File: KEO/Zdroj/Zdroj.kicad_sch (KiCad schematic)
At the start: 64 parts, among them J1 24V AC, J2 OUT, J3 Q7, Q1 BC547, Q2 BC547, Q3 BC557, Q4 BC557, Q5 BC547, Q6 BD139, Q7 2N3055, U1 TL082, U2 TL082

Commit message: OSY hw05
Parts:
- added R22, R23: 2,2K, symbol Device:R
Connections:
- net GND: now also R23.2; no longer U2.5 (+), U2.6 (-)
- net at C10.2, C7.2, C9.1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: now also R18.2; no longer R18.1
- net at C2.1, C3.2, C4.2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: now also R18.1; no longer R18.2
- net at C8.2, U1.7: now also R19.2; no longer R19.1
- net at D14.1 (K), Q5.1 (C), Q6.3 (B): now also R19.1; no longer R19.2
- net at U2.7: now also U2.6 (-)
- new net: R22.2, R23.1, U2.5 (+)
- no-connect marks 1 -> 0
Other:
- moved on the sheet: H1, H2, H3, H4, R18, R19, U2B

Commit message: OSY hw06
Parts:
- added FID1, FID2, FID3: Fiducial, Fiducial:Fiducial_0.5mm_Mask1mm, symbol Mechanical:Fiducial
- C1, C2, C4: footprint (none) -> Capacitor_THT:C_Radial_D10.0mm_H12.5mm_P5.00mm
- R1, R10, R11, R12, R13, R14, R15, R16, R17, R19, R2, R20, R21, R22, R23, R3, R4, R5, R6, R7, R8, R9, RV1, RV2: footprint (none) -> Resistor_THT:R_Axial_DIN0207_L6.3mm_D2.5mm_P7.62mm_Horizontal
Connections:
- net GND: now also C2.1, C3.2, C4.2, C5.1, C5.2, D12.2 (A), D2.2 (A), D4.2 (A), D5.1 (K), D7.2 (A), D8.1 (K), D9.1 (K), Q4.3 (E), Q5.3 (E), R10.2, R18.1, R2.2, U1.4 (V-), U2.4 (V-)
- net U1,U2+: now reaches C4.1, Q1.3 (E), Q2.2 (B), R17.1, U1.8 (V+), U2.8 (V+)
- net U1,U2+: now also R22.1
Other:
- moved on the sheet: J1

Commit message: Update Zdroj.kicad_sch
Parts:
- C10, C5: footprint (none) -> Capacitor_THT:C_Radial_D6.3mm_H5.0mm_P2.50mm
- C11, C6, C8: footprint (none) -> Capacitor_THT:C_Disc_D5.0mm_W2.5mm_P5.00mm
- C3: footprint (none) -> Capacitor_THT:C_Radial_D16.0mm_H25.0mm_P7.50mm
- C7, C9: footprint (none) -> Capacitor_THT:C_Rect_L7.0mm_W2.5mm_P5.00mm
- D10, D12, D7, D9: footprint (none) -> Diode_THT:D_DO-35_SOD27_P7.62mm_Horizontal
- J1, J2: footprint (none) -> TerminalBlock_Phoenix:TerminalBlock_Phoenix_MKDS-3-2-5.08_1x02_P5.08mm_Horizontal
- J3: footprint (none) -> TerminalBlock_Phoenix:TerminalBlock_Phoenix_MKDS-1,5-3-5.08_1x03_P5.08mm_Horizontal
- R10, RV1, RV2: footprint Resistor_THT:R_Axial_DIN0207_L6.3mm_D2.5mm_P7.62mm_Horizontal -> (none)
- R18: footprint (none) -> Resistor_THT:R_Axial_Power_L25.0mm_W6.4mm_P30.48mm
- U1, U2: footprint (none) -> Package_DIP:DIP-8_W7.62mm
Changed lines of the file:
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@@
 			)
 		)
-		(property "Footprint" "Resistor_THT:R_Axial_DIN0207_L6.3mm_D2.5mm_P7.62mm_Horizontal"
+		(property "Footprint" ""
 			(at 129.54 88.9 0)
 			(effects
@@
 			)
 		)
-		(property "Footprint" ""
+		(property "Footprint" "TerminalBlock_Phoenix:TerminalBlock_Phoenix_MKDS-1,5-3-5.08_1x03_P5.08mm_Horizontal"
 			(at 256.54 39.37 0)
 			(effects
@@
 			)
 		)
-		(property "Footprint" ""
+		(property "Footprint" "Package_DIP:DIP-8_W7.62mm"
 			(at 173.99 92.71 0)
 			(effects
@@
 			)
 		)
-		(property "Footprint" ""
+		(property "Footprint" "Capacitor_THT:C_Radial_D16.0mm_H25.0mm_P7.50mm"
 			(at 69.5452 82.55 0)
 			(effects
@@
 			)
 		)
-		(property "Footprint" ""
+		(property "Footprint" "Capacitor_THT:C_Disc_D5.0mm_W2.5mm_P5.00mm"
 			(at 267.97 86.0552 0)
 			(effects
@@
 			)
 		)
-		(property "Footprint" ""
+		(property "Footprint" "Capacitor_THT:C_Disc_D5.0mm_W2.5mm_P5.00mm"
 			(at 214.9348 77.47 0)
 			(effects
@@
 			)
 		)
-		(property "Footprint" ""
+		(property "Footprint" "Diode_THT:D_DO-35_SOD27_P7.62mm_Horizontal"
 			(at 92.71 115.57 0)
 			(effects
@@
 			)
 		)
-		(property "Footprint" ""
+		(property "Footprint" "Diode_THT:D_DO-35_SOD27_P7.62mm_Horizontal"
 			(at 224.79 124.46 0)
 			(effects
@@
 			)
 		)
-		(property "Footprint" ""
+		(property "Footprint" "Capacitor_THT:C_Rect_L7.0mm_W2.5mm_P5.00mm"
 			(at 191.4652 92.71 0)
 			(effects
@@
 			)
 		)
-		(property "Footprint" ""
+		(property "Footprint" "TerminalBlock_Phoenix:TerminalBlock_Phoenix_MKDS-3-2-5.08_1x02_P5.08mm_Horizontal"
 			(at 281.94 111.76 0)
 			(effects
@@
 			)
 		)
-		(property "Footprint" ""
+		(property "Footprint" "Package_DIP:DIP-8_W7.62mm"
 			(at 154.94 152.4 0)
 			(effects
@@
 			)
 		)
-		(property "Footprint" ""
+		(property "Footprint" "Diode_THT:D_DO-35_SOD27_P7.62mm_Horizontal"
 			(at 69.85 50.8 0)
 			(effects
@@
 			)
 		)
-		(property "Footprint" "Resistor_THT:R_Axial_DIN0207_L6.3mm_D2.5mm_P7.62mm_Horizontal"
+		(property "Footprint" ""
 			(at 127.762 105.41 90)
 			(effects
@@
 			)
 		)
-		(property "Footprint" ""
+		(property "Footprint" "Package_DIP:DIP-8_W7.62mm"
 			(at 111.76 91.44 0)
 			(effects
@@
 			)
 		)
-		(property "Footprint" ""
+		(property "Footprint" "Capacitor_THT:C_Radial_D6.3mm_H5.0mm_P2.50mm"
 			(at 105.1052 119.38 0)
 			(effects
@@
 			)
 		)
-		(property "Footprint" ""
+		(property "Footprint" "TerminalBlock_Phoenix:TerminalBlock_Phoenix_MKDS-3-2-5.08_1x02_P5.08mm_Horizontal"
 			(at 21.59 76.2 0)
 			(effects
@@
 			)
 		)
-		(property "Footprint" ""
+		(property "Footprint" "Package_DIP:DIP-8_W7.62mm"
 			(at 209.55 74.93 0)
 			(effects
@@
 			)
 		)
-		(property "Footprint" ""
+		(property "Footprint" "Resistor_THT:R_Axial_Power_L25.0mm_W6.4mm_P30.48mm"
 			(at 242.57 113.538 90)
 			(effects
@@
 			)
 		)
-		(property "Footprint" ""
+		(property "Footprint" "Capacitor_THT:C_Radial_D6.3mm_H5.0mm_P2.50mm"
 			(at 257.5052 104.14 0)
 			(effects
@@
 			)
 		)
-		(property "Footprint" ""
+		(property "Footprint" "Capacitor_THT:C_Disc_D5.0mm_W2.5mm_P5.00mm"
 			(at 109.22 102.5652 0)
 			(effects
@@
 			)
 		)
-		(property "Footprint" ""
+		(property "Footprint" "Capacitor_THT:C_Rect_L7.0mm_W2.5mm_P5.00mm"
 			(at 233.3752 62.23 0)
 			(effects
@@
 			)
 		)
-		(property "Footprint" "Resistor_THT:R_Axial_DIN0207_L6.3mm_D2.5mm_P7.62mm_Horizontal"
+		(property "Footprint" ""
 			(at 180.34 100.33 0)
 			(effects
@@
 			)
 		)
-		(property "Footprint" ""
+		(property "Footprint" "Diode_THT:D_DO-35_SOD27_P7.62mm_Horizontal"
 			(at 146.05 80.01 0)
 			(effects
@@
 			)
 		)
-		(property "Footprint" ""
+		(property "Footprint" "Package_DIP:DIP-8_W7.62mm"
 			(at 154.94 92.71 0)
 			(effects
@@
 			)
 		)
-		(property "Footprint" ""
+		(property "Footprint" "Package_DIP:DIP-8_W7.62mm"
 			(at 223.52 74.93 0)
 			(effects

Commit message: Pouzdra
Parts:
- R10: footprint (none) -> Potentiometer_THT:Potentiometer_Piher_PT-6-V_Vertical
- RV1, RV2: footprint (none) -> Potentiometer_THT:Potentiometer_Piher_PC-16_Single_Horizontal
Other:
- moved on the sheet: C2, D5, D8, J1, Q2, R4

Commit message: Téměř celá DPS
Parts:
- removed R10: 220R, Potentiometer_THT:Potentiometer_Piher_PT-6-V_Vertical, symbol Device:R_Trim
- added RV3: 220R, Potentiometer_THT:Potentiometer_Piher_PT-6-V_Vertical, symbol Device:R_Potentiometer
- C1, C2: footprint Capacitor_THT:C_Radial_D10.0mm_H12.5mm_P5.00mm -> Capacitor_THT:CP_Radial_D10.0mm_P5.00mm
- C10, C5: footprint Capacitor_THT:C_Radial_D6.3mm_H5.0mm_P2.50mm -> Capacitor_THT:CP_Radial_D6.3mm_P2.50mm
- C3: footprint Capacitor_THT:C_Radial_D16.0mm_H25.0mm_P7.50mm -> Capacitor_THT:CP_Radial_D22.0mm_P10.00mm_SnapIn
- C4: footprint Capacitor_THT:C_Radial_D10.0mm_H12.5mm_P5.00mm -> Capacitor_THT:CP_Radial_D5.0mm_P2.00mm
- R2: footprint Resistor_THT:R_Axial_DIN0207_L6.3mm_D2.5mm_P7.62mm_Horizontal -> Resistor_THT:R_Axial_DIN0414_L11.9mm_D4.5mm_P15.24mm_Horizontal
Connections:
- net GND: now also RV3.2, RV3.3; no longer C5.2, D12.2 (A), Q4.3 (E), U1.4 (V-)
- net at C10.2, C7.2, C9.1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: now also RV2.1; no longer RV2.3
- net at RV1.1: now also RV3.1; no longer R9.2
- net at RV1.3: now also R9.2
- net at D10.1 (K), R12.1, R9.1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: now also RV2.3; no longer RV2.1
- new net: C5.2, D12.2 (A), Q4.3 (E), U1.4 (V-)
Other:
- moved on the sheet: C6, RV1

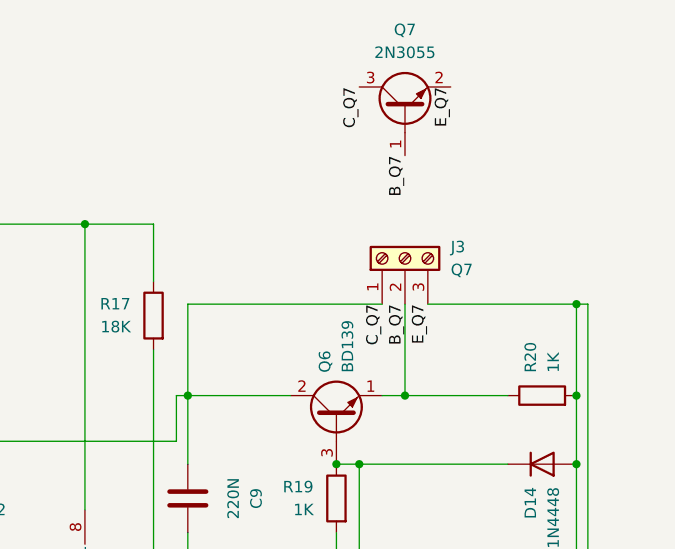
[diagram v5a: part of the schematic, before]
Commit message: Author text on PCB
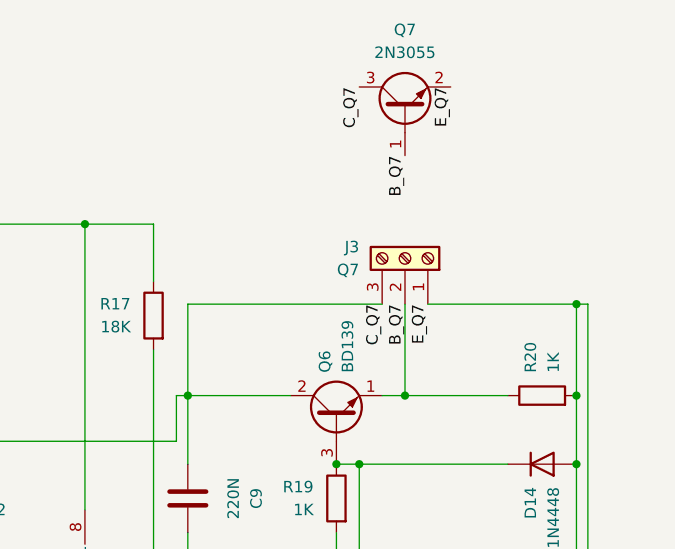
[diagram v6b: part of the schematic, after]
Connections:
- net C_Q7: now also J3.3 (Pin_3); no longer J3.1 (Pin_1)
- net E_Q7: now also J3.1 (Pin_1); no longer J3.3 (Pin_3)
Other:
- moved on the sheet: J3
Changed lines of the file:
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@@
 	(title_block
 		(title "${TITLE}")
-		(date "2025-11-16")
+		(date "2025-11-17")
 		(rev "${REV}")
 		(company "${AUTHOR}")
@@
 	(symbol
 		(lib_id "Connector:Screw_Terminal_01x03")
-		(at 256.54 39.37 90)
+		(at 256.54 39.37 270)
+		(mirror x)
 		(unit 1)
 		(exclude_from_sim no)
@@
 		(on_board yes)
 		(dnp no)
-		(fields_autoplaced yes)
 		(property "Reference" "J3"
-			(at 261.62 38.0999 90)
+			(at 251.46 38.0999 90)
 			(effects
 				(font
@@
 		)
 		(property "Value" "Q7"
-			(at 261.62 40.6399 90)
-			(effects
-				(font
+			(at 251.46 40.6399 90)
+			(effects
+				(font

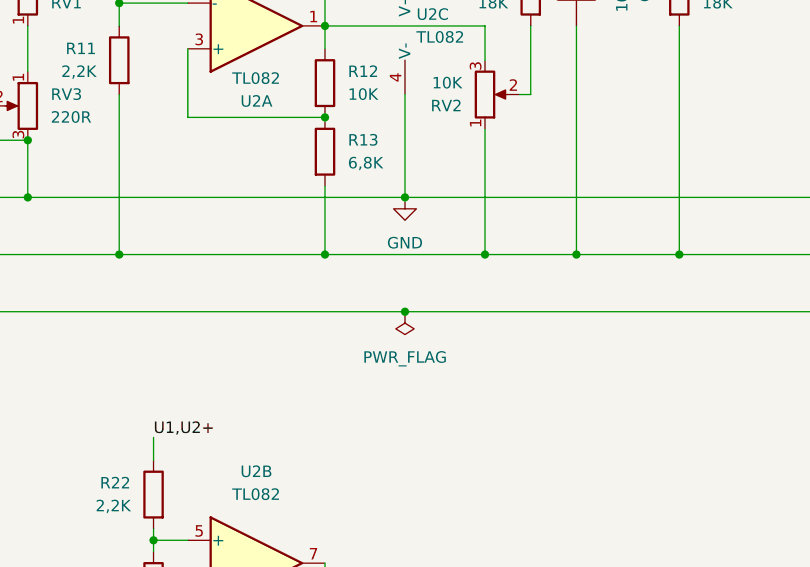
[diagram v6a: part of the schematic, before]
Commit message: KEO GND
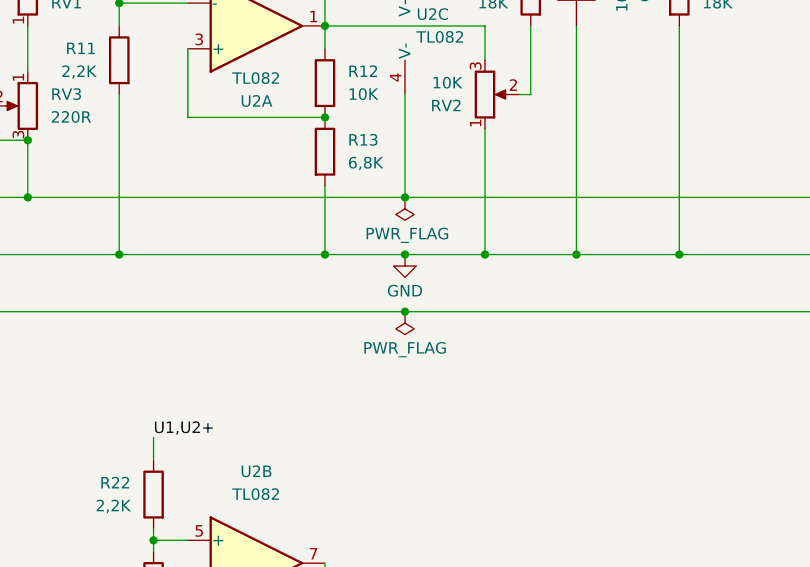
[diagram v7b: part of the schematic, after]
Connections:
- net GND: now also C10.2, C7.2, C9.1, D13.2 (A), J2.1 (Pin_1), R11.2, R13.2, R16.2, R18.2, R8.2, RV2.1; no longer C2.1, C3.2, C4.2, C5.1, D2.2 (A), D4.2 (A), D5.1 (K), D7.2 (A), D8.1 (K), D9.1 (K), Q5.3 (E), R18.1, R2.2, RV3.2, RV3.3, U2.4 (V-)
- new net: C2.1, C3.2, C4.2, C5.1, D2.2 (A), D4.2 (A), D5.1 (K), D7.2 (A), D8.1 (K), D9.1 (K), Q5.3 (E), R18.1, R2.2, RV3.2, RV3.3, U2.4 (V-)
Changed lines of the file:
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@@
 	)
 	(junction
+		(at 171.45 118.11)
+		(diameter 0)
+		(color 0 0 0 0)
+	)
+	(junction
 		(at 201.93 85.09)
 		(diameter 0)
@@
 	(wire
 		(pts
-			(xy 162.56 118.11) (xy 180.34 118.11)
+			(xy 162.56 118.11) (xy 171.45 118.11)
 		)
 		(stroke
@@
 	(wire
 		(pts
+			(xy 171.45 118.11) (xy 180.34 118.11)
+		)
+		(stroke
+			(width 0)
+			(type default)
+		)
+	)
+	(wire
+		(pts
 			(xy 119.38 88.9) (xy 125.73 88.9)
 		)
@@
 	(symbol
 		(lib_id "power:GND")
-		(at 171.45 111.76 0)
+		(at 171.45 118.11 0)
 		(unit 1)
 		(exclude_from_sim no)
@@
 		(on_board yes)
 		(dnp no)
-		(fields_autoplaced yes)
 		(property "Reference" "#PWR010"
-			(at 171.45 118.11 0)
+			(at 171.45 124.46 0)
 			(effects
 				(font
@@
 		)
 		(property "Value" "GND"
-			(at 171.45 116.84 0)
+			(at 171.45 122.174 0)
 			(effects
 				(font
@@
 		)
 		(property "Footprint" ""
-			(at 171.45 111.76 0)
+			(at 171.45 118.11 0)
 			(effects
 				(font
@@
 		)
 		(property "Datasheet" ""
-			(at 171.45 111.76 0)
+			(at 171.45 118.11 0)
 			(effects
 				(font
@@
 		)
 		(property "Description" "Power symbol creates a global label with name \"GND\" , ground"
-			(at 171.45 111.76 0)
+			(at 171.45 118.11 0)
 			(effects
 				(font
@@
 		(on_board yes)
 		(dnp no)
-		(fields_autoplaced yes)
 		(property "Reference" "#FLG01"
 			(at 171.45 126.365 0)
@@
 		)
 		(property "Value" "PWR_FLAG"
-			(at 171.45 129.54 0)
+			(at 171.45 128.524 0)
 			(effects
 				(font
@@
 					(unit 1)
 				)
+			)
+		)
+	)
+	(symbol
+		(lib_id "power:PWR_FLAG")
+		(at 171.45 111.76 180)
+		(unit 1)
+		(exclude_from_sim no)
+		(in_bom yes)
+		(on_board yes)
+		(dnp no)
+		(property "Reference" "#FLG04"
+			(at 171.45 113.665 0)
+			(effects
+				(font
+					(size 1.27 1.27)
+				)
+				(hide yes)
+			)
+		)
+		(property "Value" "PWR_FLAG"
+			(at 171.704 115.824 0)
+			(effects
+				(font
+					(size 1.27 1.27)
+				)
+			)
+		)
+		(property "Footprint" ""
+			(at 171.45 111.76 0)
+			(effects
+				(font
+					(size 1.27 1.27)
+				)
+				(hide yes)
+			)
+		)
+		(property "Datasheet" "~"
+			(at 171.45 111.76 0)
+			(effects
+				(font
+					(size 1.27 1.27)
+				)
+				(hide yes)
+			)
+		)
+		(property "Description" "Special symbol for telling ERC where power comes from"
+			(at 171.45 111.76 0)
+			(effects
+				(font
+					(size 1.27 1.27)
+				)
+				(hide yes)
+			)
+		)
+		(pin "1"
+		)
+		(instances
+			(project "Zdroj"
+				(path "/b0153651-e2ef-4a9d-ae62-4f00bceb77f7"
+					(reference "#FLG04")
+					(unit 1)
+				)

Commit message: KEO Drobné úpravy
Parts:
- removed FID3: Fiducial, Fiducial:Fiducial_0.5mm_Mask1mm, symbol Mechanical:Fiducial
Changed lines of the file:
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@@
-	(symbol
-		(lib_id "Mechanical:Fiducial")
-		(at 69.85 157.48 0)
-		(unit 1)
-		(exclude_from_sim no)
-		(in_bom no)
-		(on_board yes)
-		(dnp no)
-		(fields_autoplaced yes)
-		(property "Reference" "FID3"
-			(at 72.39 156.2099 0)
-			(effects
-				(font
-					(size 1.27 1.27)
-				)
-				(justify left)
-			)
-		)
-		(property "Value" "Fiducial"
-			(at 72.39 158.7499 0)
-			(effects
-				(font
-					(size 1.27 1.27)
-				)
-				(justify left)
-			)
-		)
-		(property "Footprint" "Fiducial:Fiducial_0.5mm_Mask1mm"
-			(at 69.85 157.48 0)
-			(effects
-				(font
-					(size 1.27 1.27)
-				)
-				(hide yes)
-			)
-		)
-		(property "Datasheet" "~"
-			(at 69.85 157.48 0)
-			(effects
-				(font
-					(size 1.27 1.27)
-				)
-				(hide yes)
-			)
-		)
-		(property "Description" "Fiducial Marker"
-			(at 69.85 157.48 0)
-			(effects
-				(font
-					(size 1.27 1.27)
-				)
-				(hide yes)
-			)
-		)
-		(instances
-			(project "Zdroj"
-				(path "/b0153651-e2ef-4a9d-ae62-4f00bceb77f7"
-					(reference "FID3")
-					(unit 1)
-				)
-			)
-		)
-	)
 	(symbol
 		(lib_id "Mechanical:Fiducial")
